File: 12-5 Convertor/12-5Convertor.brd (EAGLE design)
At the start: 31.4 x 52.7 mm, 7 parts, among them U1 LM2678

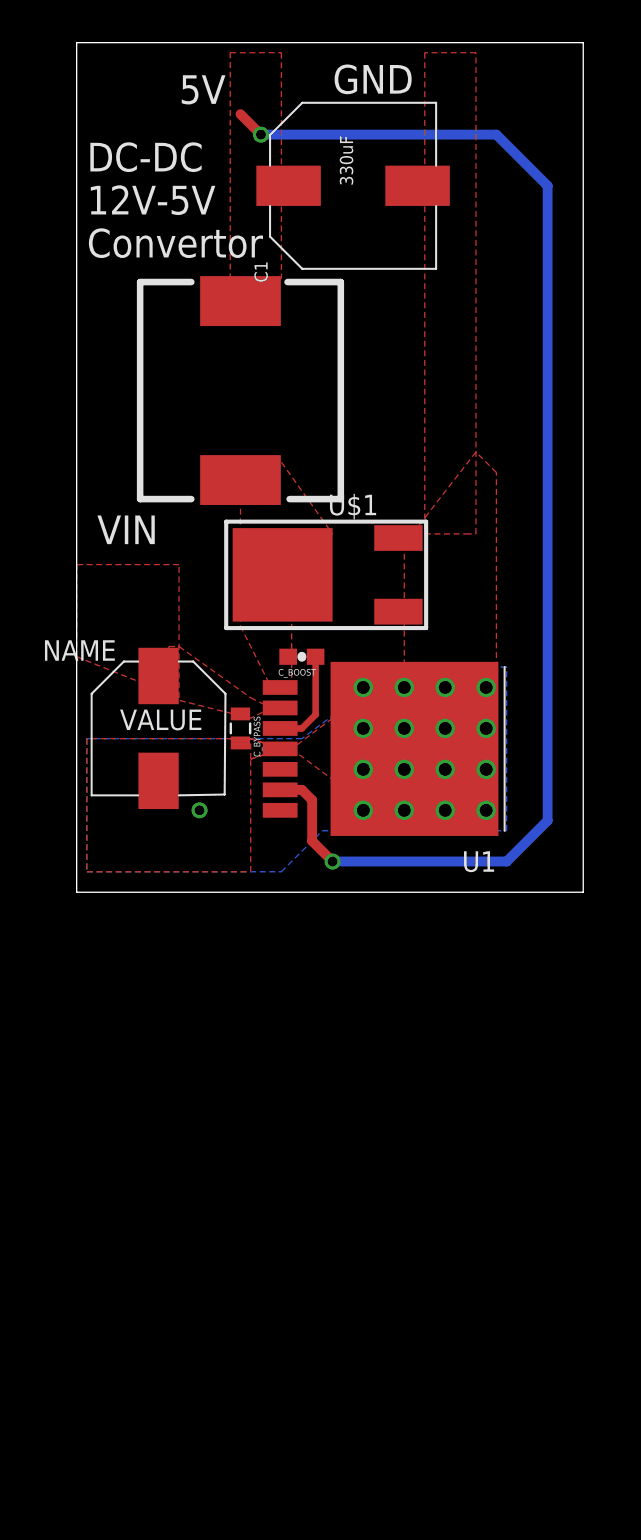
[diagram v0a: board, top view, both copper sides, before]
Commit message: adjust the dc-dc 12-5 convertor
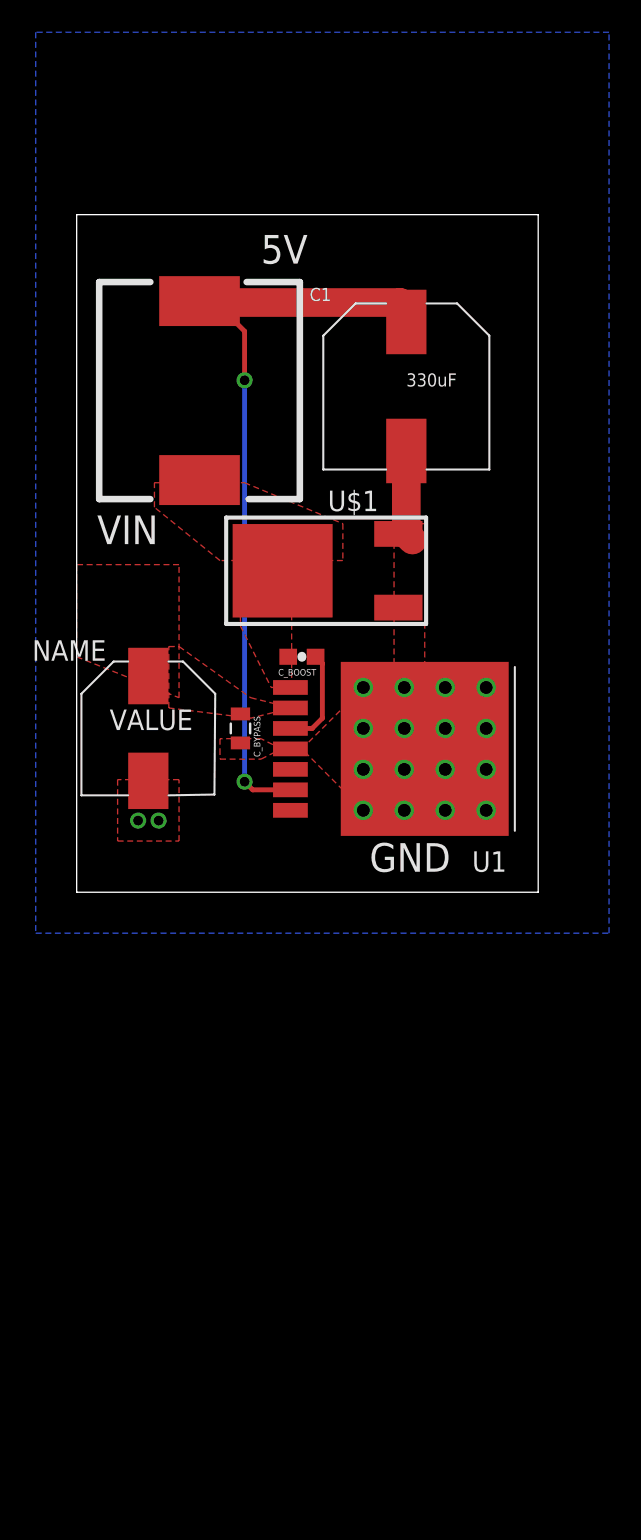
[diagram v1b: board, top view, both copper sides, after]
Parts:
- moved C1 12.9 mm to (53.5, 46.6), turned to 0 degrees
- moved L1 2.54 mm to (40.6, 46.4)
- moved C_IN 0.63 mm to (37.5, 25.4)
- moved U1 0.63 mm to (54.6, 24.1)
- moved U$1 0.25 mm to (48.9, 35.2)
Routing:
- net 5V: track 81.2 -> 48.2 mm
- net GND: track 0.00 -> 5.68 mm, vias 17 -> 18
- removed copper zone on layer 1, net 5V
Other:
- board size 31.4 x 52.7 mm -> 28.6 x 42 mm
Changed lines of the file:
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@@
 <setting verticaltext="up"/>
 </settings>
-<grid distance="0.1" unitdist="inch" unit="inch" style="lines" multiple="1" display="no" altdistance="0.025" altunitdist="inch" altunit="inch"/>
+<grid distance="0.01" unitdist="inch" unit="inch" style="lines" multiple="1" display="yes" altdistance="0.025" altunitdist="inch" altunit="inch"/>
 <layers>
 <layer number="1" name="Top" color="4" fill="1" visible="yes" active="yes"/>
@@
 <board>
 <plain>
-<wire x1="33.02" y1="15.24" x2="64.44" y2="15.24" width="0" layer="20"/>
-<wire x1="64.44" y1="15.24" x2="64.44" y2="67.935" width="0" layer="20"/>
-<wire x1="64.44" y1="67.935" x2="33.02" y2="67.935" width="0" layer="20"/>
-<wire x1="33.02" y1="67.935" x2="33.02" y2="15.24" width="0" layer="20"/>
+<wire x1="33.02" y1="15.24" x2="61.646" y2="15.24" width="0" layer="20"/>
+<wire x1="61.646" y1="15.24" x2="61.646" y2="57.267" width="0" layer="20"/>
+<wire x1="61.646" y1="57.267" x2="33.02" y2="57.267" width="0" layer="20"/>
+<wire x1="33.02" y1="57.267" x2="33.02" y2="15.24" width="0" layer="20"/>
 <text x="34.29" y="36.83" size="1.778" layer="21">VIN</text>
-<text x="39.37" y="64.135" size="1.778" layer="21">5V</text>
-<text x="48.895" y="64.77" size="1.778" layer="21">GND</text>
-<text x="33.655" y="54.61" size="1.778" layer="21">DC-DC
+<text x="44.45" y="54.229" size="1.778" layer="21">5V</text>
+<text x="51.181" y="16.51" size="1.778" layer="21">GND</text>
+<text x="36.195" y="42.672" size="1.778" layer="22">DC-DC
 12V-5V
 Convertor</text>
@@
 </autorouter>
 <elements>
-<element name="C1" library="PowerComponents" package="CPOL-US(10.3_10.3MM)" value="330uF" x="50.165" y="59.055" rot="R90"/>
+<element name="C1" library="PowerComponents" package="CPOL-US(10.3_10.3MM)" value="330uF" x="53.467" y="46.609"/>
 <element name="C_BOOST" library="SparkFun-Passives" package="0603-CAP" value="0.01uF" x="46.99" y="29.845" rot="R180"/>
-<element name="C_IN" library="PowerComponents" package="CPOL-US(8.3_8.3MM)" value="C-ALUMINUM(47UF)" x="38.1" y="25.4"/>
+<element name="C_IN" library="PowerComponents" package="CPOL-US(8.3_8.3MM)" value="C-ALUMINUM(47UF)" x="37.465" y="25.4"/>
 <element name="C_BYPASS" library="SparkFun-Capacitors" package="0805" value="0.47uF" x="43.18" y="25.4" rot="R270"/>
-<element name="L1" library="DiscreteComponents" package="SRP1265A" value="22uH" x="43.18" y="46.355" rot="R90"/>
-<element name="U$1" library="PowerComponents" package="DPAK-3" value="SWITCHMODE_SCHOTTKY" x="48.895" y="34.925"/>
-<element name="U1" library="PowerComponents" package="LM2678" value="LM2678" x="53.975" y="24.13" rot="R180"/>
+<element name="L1" library="DiscreteComponents" package="SRP1265A" value="22uH" x="40.64" y="46.355" rot="R90"/>
+<element name="U$1" library="PowerComponents" package="DPAK-3" value="SWITCHMODE_SCHOTTKY" x="48.895" y="35.179"/>
+<element name="U1" library="PowerComponents" package="LM2678" value="LM2678" x="54.61" y="24.13" rot="R180"/>
 </elements>
 <signals>
@@
 <vertex x="39.37" y="30.48"/>
 <vertex x="43.815" y="27.305"/>
-<vertex x="45.085" y="26.67"/>
+<vertex x="46.355" y="26.67"/>
 <vertex x="43.815" y="26.035"/>
-<vertex x="38.735" y="27.305"/>
+<vertex x="38.735" y="26.67"/>
 <vertex x="38.735" y="30.48"/>
 </polygon>
@@
 <contactref element="U1" pad="3"/>
 <contactref element="C_BOOST" pad="1"/>
-<wire x1="47.84" y1="29.845" x2="47.84" y2="26.25" width="0.4064" layer="1"/>
-<wire x1="47.84" y1="26.25" x2="46.99" y2="25.4" width="0.4064" layer="1"/>
-<wire x1="46.99" y1="25.4" x2="45.6438" y2="25.4" width="0.4064" layer="1"/>
+<wire x1="46.2788" y1="25.4" x2="47.625" y2="25.4" width="0.3048" layer="1"/>
+<wire x1="47.625" y1="25.4" x2="48.26" y2="26.035" width="0.3048" layer="1"/>
+<wire x1="48.26" y1="26.035" x2="48.26" y2="29.425" width="0.3048" layer="1"/>
+<wire x1="48.26" y1="29.425" x2="47.84" y2="29.845" width="0.3048" layer="1"/>
 </signal>
 <signal name="N$3">
@@
 </polygon>
 <polygon width="0.254" layer="1" thermals="no">
-<vertex x="43.18" y="37.465"/>
-<vertex x="43.18" y="40.64"/>
-<vertex x="45.72" y="41.91"/>
-<vertex x="48.895" y="37.465"/>
+<vertex x="37.846" y="40.64"/>
+<vertex x="43.434" y="40.64"/>
+<vertex x="49.53" y="38.1"/>
+<vertex x="49.53" y="35.814"/>
+<vertex x="41.91" y="35.814"/>
+<vertex x="37.846" y="39.116"/>
 </polygon>
 </signal>
@@
 <contactref element="L1" pad="P$2"/>
 <contactref element="C1" pad="+"/>
-<wire x1="45.6438" y1="21.59" x2="46.99" y2="21.59" width="0.6096" layer="1"/>
-<wire x1="46.99" y1="21.59" x2="47.625" y2="20.955" width="0.6096" layer="1"/>
-<wire x1="47.625" y1="20.955" x2="47.625" y2="18.415" width="0.6096" layer="1"/>
-<wire x1="47.625" y1="18.415" x2="48.895" y2="17.145" width="0.6096" layer="1"/>
-<via x="48.895" y="17.145" extent="1-16" drill="0.6"/>
-<wire x1="48.895" y1="17.145" x2="59.69" y2="17.145" width="0.6096" layer="16"/>
-<wire x1="59.69" y1="17.145" x2="62.23" y2="19.685" width="0.6096" layer="16"/>
-<wire x1="62.23" y1="19.685" x2="62.23" y2="59.055" width="0.6096" layer="16"/>
-<polygon width="0.254" layer="1" thermals="no">
-<vertex x="42.545" y="52.07"/>
-<vertex x="42.545" y="67.31"/>
-<vertex x="45.72" y="67.31"/>
-<vertex x="45.72" y="53.34"/>
-<vertex x="44.45" y="52.07"/>
-</polygon>
-<wire x1="62.23" y1="59.055" x2="59.055" y2="62.23" width="0.6096" layer="16"/>
-<wire x1="59.055" y1="62.23" x2="44.45" y2="62.23" width="0.6096" layer="16"/>
-<via x="44.45" y="62.23" extent="1-16" drill="0.6"/>
-<wire x1="44.45" y1="62.23" x2="43.18" y2="63.5" width="0.6096" layer="1"/>
+<wire x1="53.467" y1="50.609" x2="53.467" y2="51.435" width="1.778" layer="1"/>
+<wire x1="53.467" y1="51.435" x2="53.086" y2="51.816" width="1.778" layer="1"/>
+<wire x1="53.086" y1="51.816" x2="41.402" y2="51.816" width="1.778" layer="1"/>
+<wire x1="41.402" y1="51.816" x2="41.275" y2="51.689" width="1.778" layer="1"/>
+<wire x1="41.275" y1="51.689" x2="41.148" y2="51.562" width="1.778" layer="1"/>
+<wire x1="41.148" y1="51.562" x2="40.9829" y2="51.562" width="1.778" layer="1"/>
+<wire x1="40.9829" y1="51.562" x2="40.64" y2="51.9049" width="1.778" layer="1"/>
+<wire x1="41.402" y1="51.816" x2="41.402" y2="52.07" width="1.778" layer="1"/>
+<wire x1="46.2788" y1="21.59" x2="43.942" y2="21.59" width="0.3048" layer="1"/>
+<wire x1="43.942" y1="21.59" x2="43.434" y2="22.098" width="0.3048" layer="1"/>
+<via x="43.434" y="22.098" extent="1-16" drill="0.6"/>
+<wire x1="43.434" y1="22.098" x2="43.434" y2="46.99" width="0.3048" layer="16"/>
+<via x="43.434" y="46.99" extent="1-16" drill="0.6"/>
+<wire x1="43.434" y1="46.99" x2="43.434" y2="50.038" width="0.3048" layer="1"/>
+<wire x1="43.434" y1="50.038" x2="42.164" y2="51.308" width="0.3048" layer="1"/>
+<wire x1="42.164" y1="51.308" x2="41.656" y2="51.308" width="0.3048" layer="1"/>
+<wire x1="41.656" y1="51.308" x2="41.275" y2="51.689" width="0.3048" layer="1"/>
 </signal>
 <signal name="GND">
@@
 <contactref element="U$1" pad="P$1"/>
 <contactref element="U1" pad="TAB"/>
-<polygon width="0.254" layer="1" thermals="no">
-<vertex x="48.895" y="26.035"/>
-<vertex x="46.355" y="24.13"/>
-<vertex x="48.895" y="22.225"/>
-</polygon>
-<polygon width="0.254" layer="1">
-<vertex x="45.72" y="24.13"/>
-<vertex x="43.815" y="24.765"/>
-<vertex x="33.655" y="24.765"/>
-<vertex x="33.655" y="16.51"/>
-<vertex x="43.815" y="16.51"/>
-<vertex x="43.815" y="23.495"/>
-</polygon>
-<polygon width="0.254" layer="1" thermals="no">
-<vertex x="45.72" y="24.13"/>
-<vertex x="43.815" y="23.495"/>
-<vertex x="43.815" y="24.765"/>
-</polygon>
-<polygon width="0.254" layer="1" thermals="no">
-<vertex x="53.34" y="36.83"/>
-<vertex x="53.34" y="28.575"/>
-<vertex x="59.055" y="28.575"/>
-<vertex x="59.055" y="41.275"/>
-<vertex x="57.785" y="42.545"/>
-</polygon>
-<polygon width="0.254" layer="16" thermals="no">
-<vertex x="59.69" y="29.21"/>
-<vertex x="49.53" y="29.21"/>
-<vertex x="49.53" y="26.67"/>
-<vertex x="46.99" y="24.765"/>
-<vertex x="33.655" y="24.765"/>
-<vertex x="33.655" y="16.51"/>
-<vertex x="45.72" y="16.51"/>
-<vertex x="48.26" y="19.05"/>
-<vertex x="59.69" y="19.05"/>
-</polygon>
 <via x="50.8" y="25.4" extent="1-16" drill="0.8"/>
 <via x="50.8" y="22.86" extent="1-16" drill="0.8"/>
@@
 <via x="55.88" y="27.94" extent="1-16" drill="0.8"/>
 <via x="55.88" y="25.4" extent="1-16" drill="0.8"/>
-<via x="40.64" y="20.32" extent="1-16" drill="0.6"/>
-<polygon width="0.254" layer="1" thermals="no">
-<vertex x="54.61" y="67.31"/>
-<vertex x="54.61" y="37.465"/>
-<vertex x="57.15" y="37.465"/>
-<vertex x="57.785" y="37.465"/>
-<vertex x="57.785" y="67.31"/>
-</polygon>
+<via x="36.83" y="19.685" extent="1-16" drill="0.6"/>
+<polygon width="0.3048" layer="16">
+<vertex x="30.48" y="12.7"/>
+<vertex x="66.04" y="12.7"/>
+<vertex x="66.04" y="68.58"/>
+<vertex x="30.48" y="68.58"/>
+</polygon>
+<polygon width="0.3048" layer="1" thermals="no">
+<vertex x="52.705" y="38.1"/>
+<vertex x="52.705" y="29.21"/>
+<vertex x="54.61" y="29.21"/>
+<vertex x="54.61" y="38.1"/>
+</polygon>
+<polygon width="0.3048" layer="1" thermals="no">
+<vertex x="50.8" y="20.32"/>
+<vertex x="46.99" y="24.13"/>
+<vertex x="50.165" y="27.305"/>
+</polygon>
+<polygon width="0.3048" layer="1" thermals="no">
+<vertex x="45.72" y="24.13"/>
+<vertex x="44.45" y="24.765"/>
+<vertex x="41.91" y="24.765"/>
+<vertex x="41.91" y="24.13"/>
+<vertex x="41.91" y="23.495"/>
+<vertex x="44.45" y="23.495"/>
+</polygon>
+<polygon width="0.3048" layer="1" thermals="no">
+<vertex x="35.56" y="22.225"/>
+<vertex x="35.56" y="18.415"/>
+<vertex x="39.37" y="18.415"/>
+<vertex x="39.37" y="22.225"/>
+</polygon>
+<via x="38.1" y="19.685" extent="1-16" drill="0.6"/>
+<wire x1="53.467" y1="42.609" x2="53.467" y2="37.465" width="1.778" layer="1"/>
+<wire x1="53.467" y1="37.465" x2="53.848" y2="37.084" width="1.778" layer="1"/>
 </signal>
 </signals>
